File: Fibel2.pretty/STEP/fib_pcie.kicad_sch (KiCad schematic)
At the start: 57 parts, among them J901 Bus_M.2_2199230-6, J902 Bus_M.2_1-2199230-6, M901 Mech_M2_2280_H2.5mm, Y901 Oscillator_SMD_32.768kHz_ECS_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

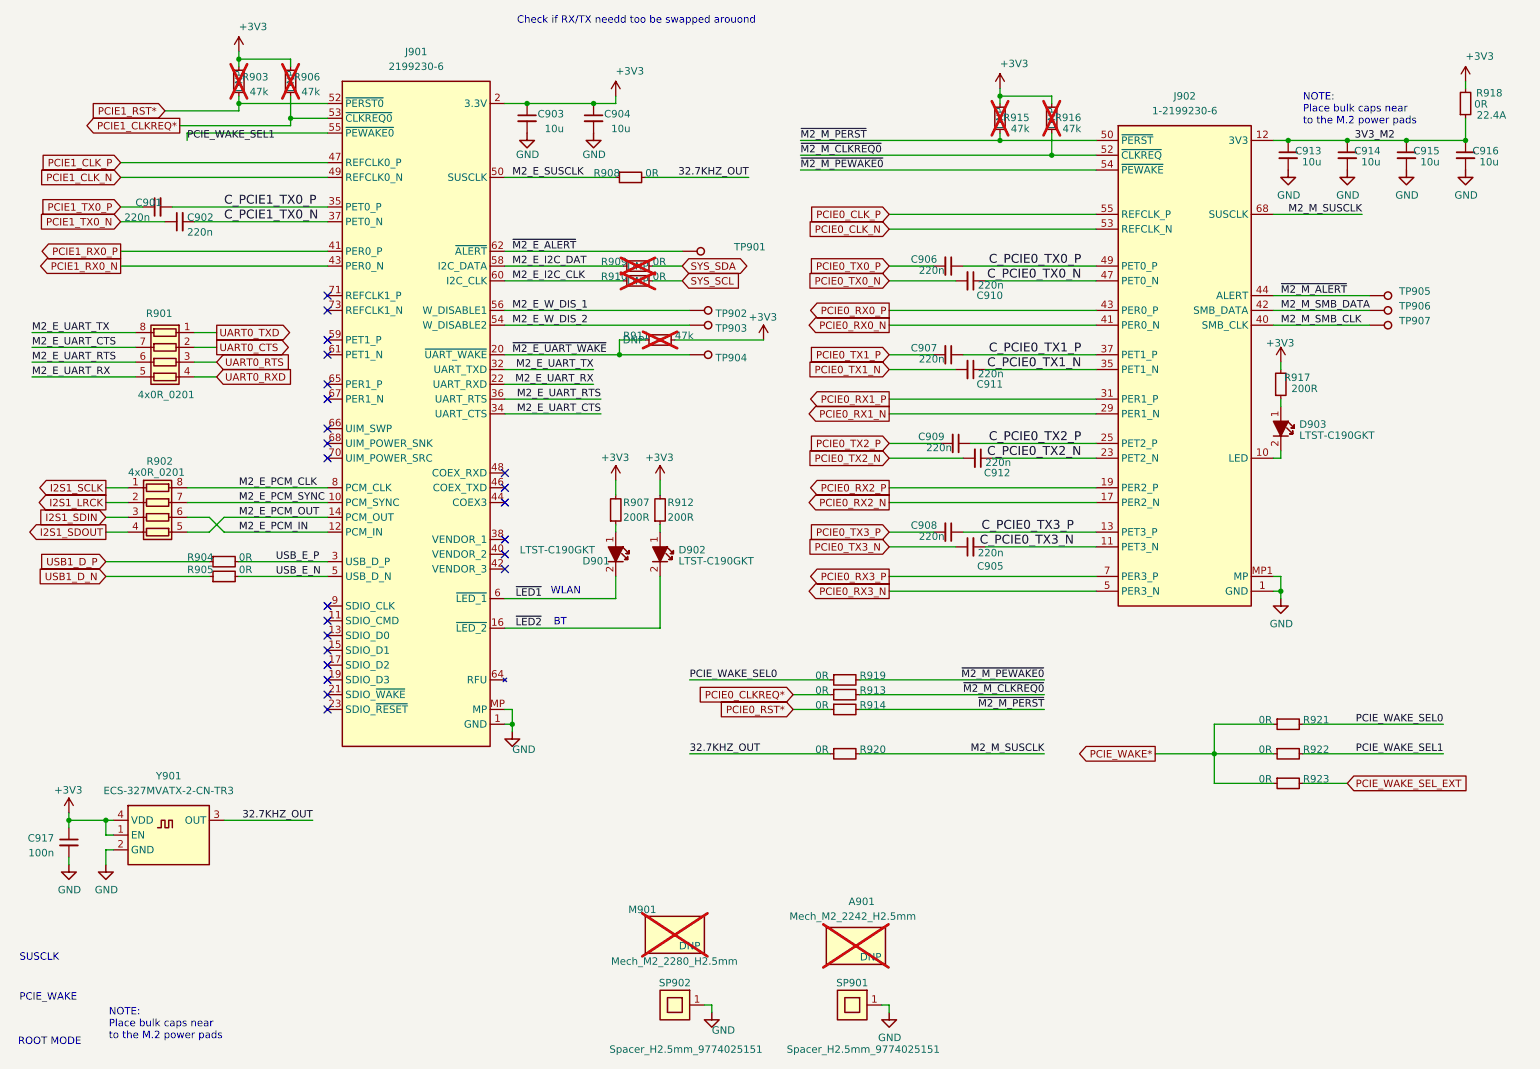
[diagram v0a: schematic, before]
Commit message: refactored PCIe pages
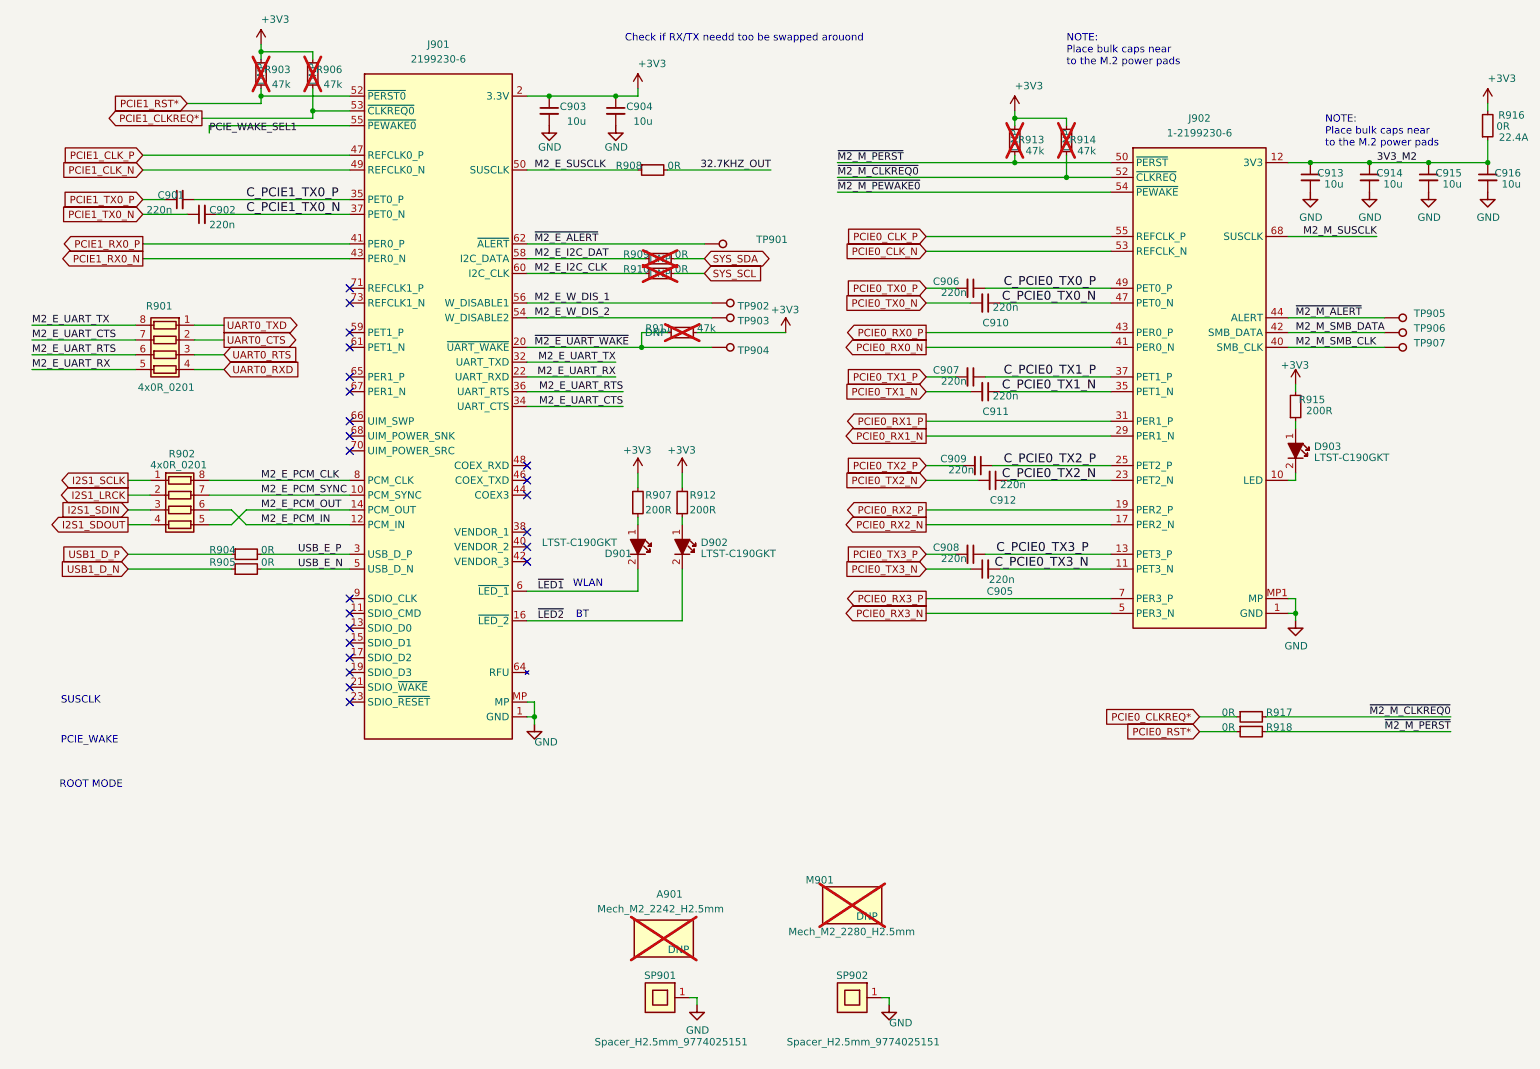
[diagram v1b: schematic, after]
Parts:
- removed C917: C_100n_0402, jetson-orin-baseboard-footprints:C_0402_1005Metric, symbol jetson-orin-baseboard:C_100n_0402
- removed R913, R914, R919, R920, R921, R922, R923: R_0R_0402, jetson-orin-baseboard-footprints:R_0402_1005Metric, symbol jetson-orin-baseboard:R_0R_0402
- removed R915, R916: 47K, Resistor_SMD:R_0603_1608Metric, symbol jetson-orin-baseboard:R_47k_0402
- removed R917: 200R, Resistor_SMD:R_0603_1608Metric, symbol jetson-orin-baseboard:R_200R_0402
- removed R918: 0R 22A, Resistor_SMD:R_0603_1608Metric, symbol jetson-orin-baseboard:R_0R_22.4A_0603
- removed Y901: Oscillator_SMD_32.768kHz_ECS_2520MV, jetson-orin-baseboard-footprints:Oscillator_SMD_ECS_2520MV_2.5x2mm, symbol jetson-orin-baseboard:Oscillator_32.768kHz_ECS_2520MV
- added R913, R914: 47K, Resistor_SMD:R_0603_1608Metric, symbol jetson-orin-baseboard:R_47k_0402
- added R915: 200R, Resistor_SMD:R_0603_1608Metric, symbol jetson-orin-baseboard:R_200R_0402
- added R916: 0R 22A, Resistor_SMD:R_0603_1608Metric, symbol jetson-orin-baseboard:R_0R_22.4A_0603
- added R917, R918: R_0R_0402, jetson-orin-baseboard-footprints:R_0402_1005Metric, symbol jetson-orin-baseboard:R_0R_0402
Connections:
- net +3V3: now also R913.1, R914.1, R915.2, R916.2
- net 3V3_M2: now also R916.1
- net PCIE0_CLKREQ*: now also R917.1
- net PCIE0_RST*: now also R918.1
- net ~{M2_M_CLKREQ0}: now also R914.2, R917.2
- net ~{M2_M_PERST}: now also R913.2, R918.2
- net at D903.1: now also R915.1
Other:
- moved on the sheet: A901, C901, C902, C903, C904, D901, D902, J901, R901, R902, R903, R904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
